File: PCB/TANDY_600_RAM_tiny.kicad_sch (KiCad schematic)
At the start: 5 parts, among them J1 DIN 41612 2x22 male right-ang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, U1 628128_TSOP, U2 74HC08

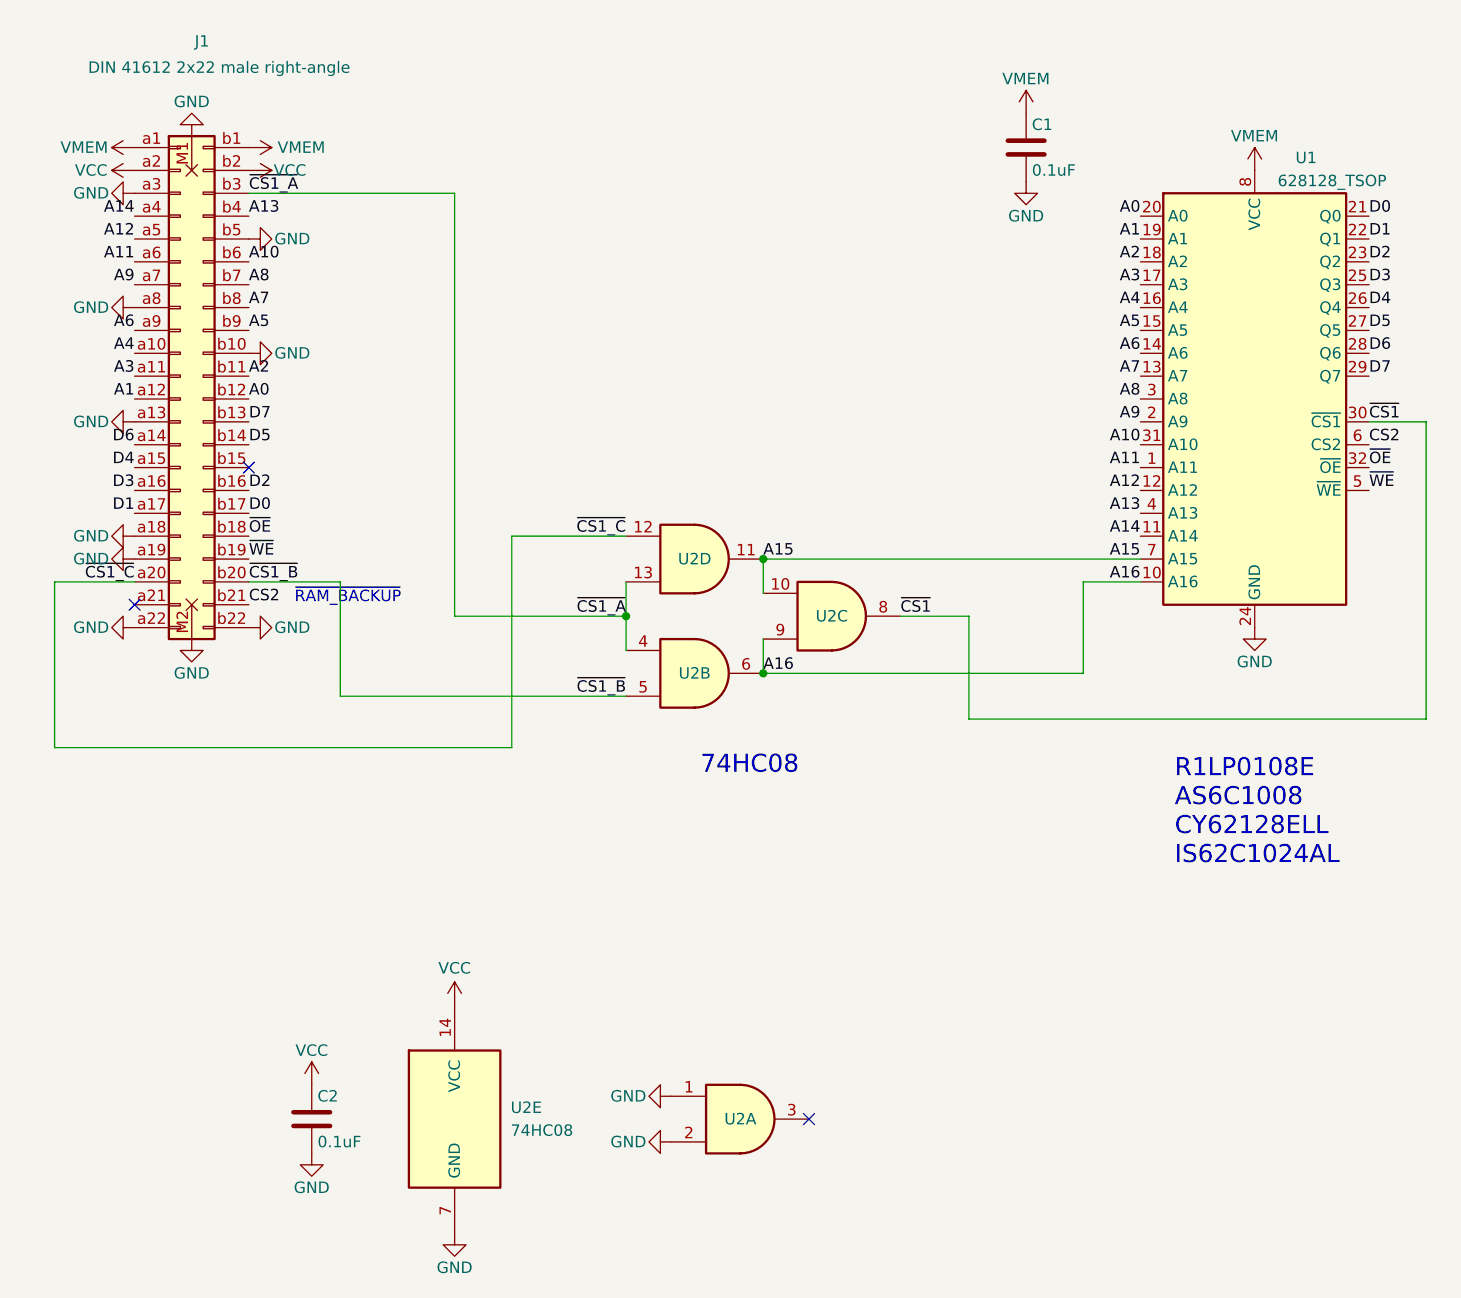
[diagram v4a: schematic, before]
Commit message: footprints on tiny
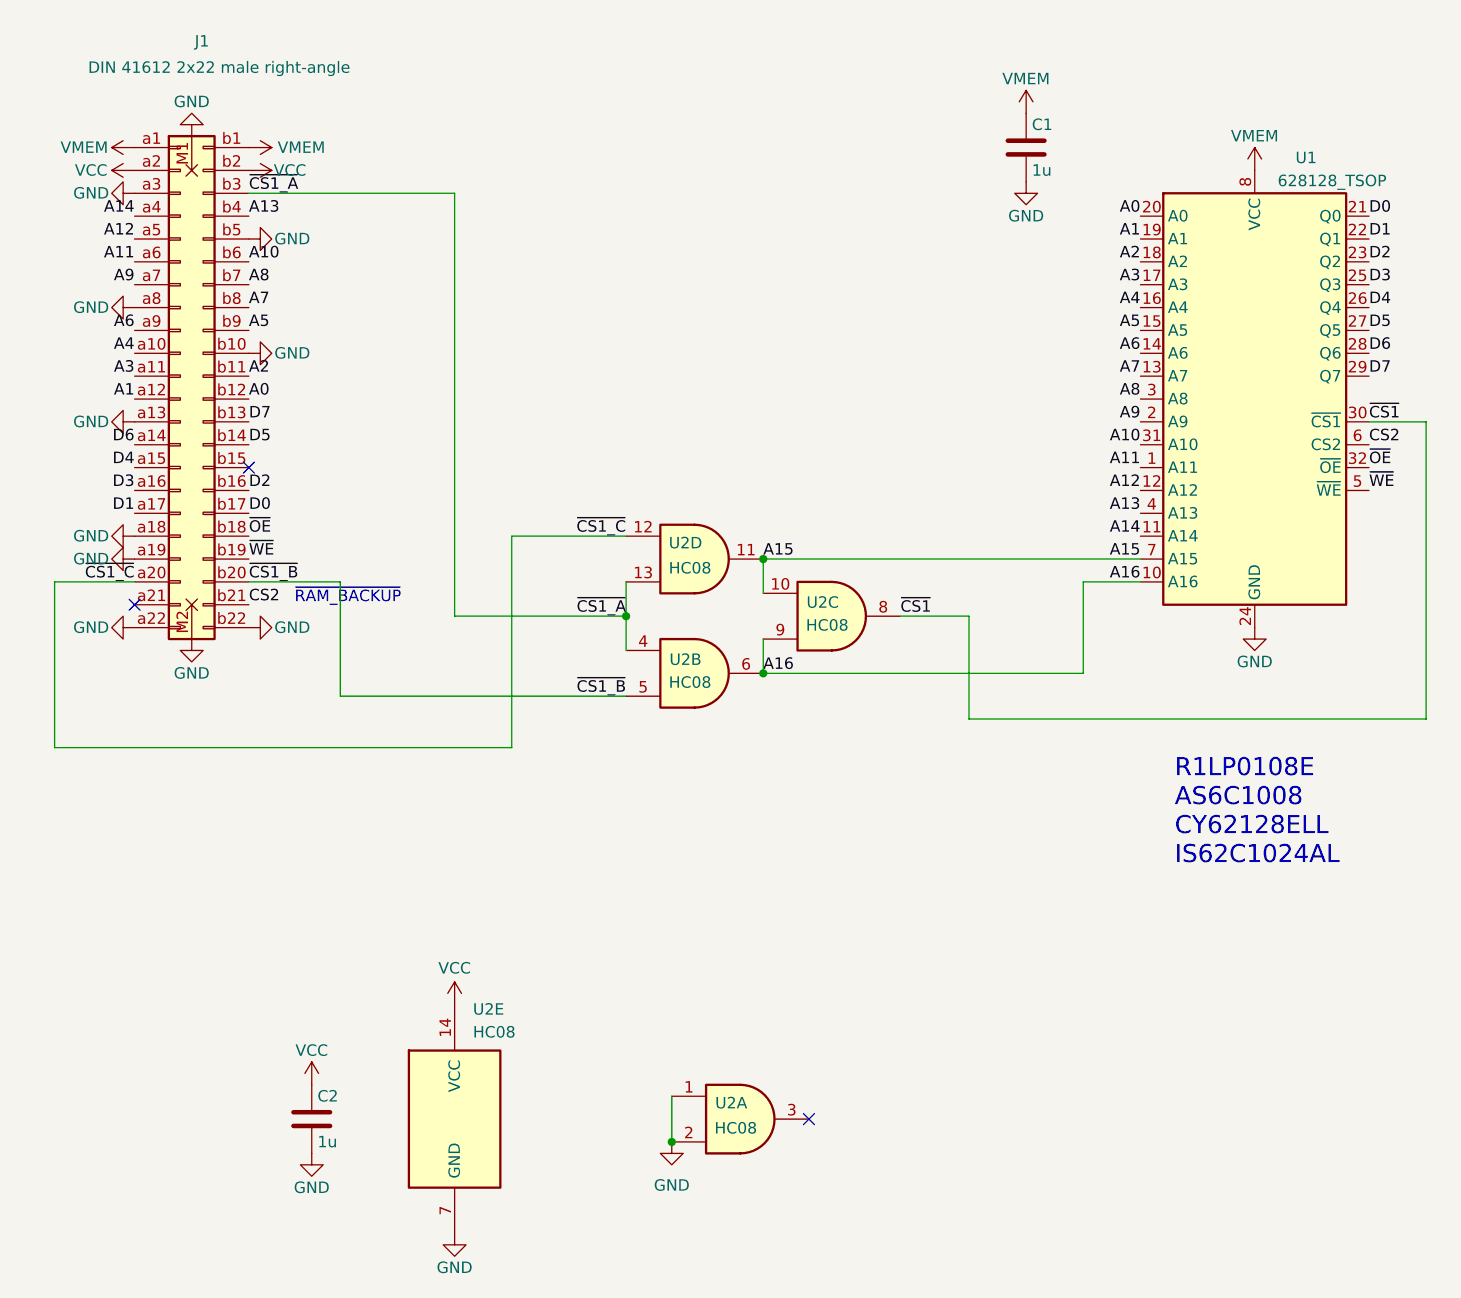
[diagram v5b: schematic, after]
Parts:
- C1, C2: value 0.1uF -> 1u
- U2: value 74HC08 -> HC08
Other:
- note removed: "74HC08"

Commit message: datasheets OPRM pinout
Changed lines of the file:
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@@
 (kicad_sch
-	(version 20231120)
+	(version 20250114)
 	(generator "eeschema")
-	(generator_version "8.0")
+	(generator_version "9.0")
 	(paper "USLetter")
 	(title_block
@@
 		(comment 3 "Replaces TANDY Cat. No. 26-3910 \"OPRM\"")
 	)
+	(text "~{RAM_BACKUP}"
+		(exclude_from_sim no)
+		(at 83.82 101.6 0)
+		(effects
+			(font
+				(size 1.27 1.27)
+			)
+			(justify left bottom)
+		)
+	)
+	(text "R1LP0108E\nAS6C1008\nCY62128ELL\nIS62C1024AL\n"
+		(exclude_from_sim no)
+		(at 181.61 130.683 0)
+		(effects
+			(font
+				(size 2 2)
+			)
+			(justify left bottom)
+		)
+	)
 	(junction
 		(at 135.89 96.52)
@@
 		)
 	)
-	(text "~{RAM_BACKUP}"
-		(exclude_from_sim no)
-		(at 83.82 101.6 0)
-		(effects
-			(font
-				(size 1.27 1.27)
-			)
-			(justify left bottom)
-		)
-	)
-	(text "R1LP0108E\nAS6C1008\nCY62128ELL\nIS62C1024AL\n"
-		(exclude_from_sim no)
-		(at 181.61 130.683 0)
-		(effects
-			(font
-				(size 2 2)
-			)
-			(justify left bottom)
-		)
-	)
 	(label "D2"
 		(at 78.74 88.9 0)
-		(fields_autoplaced yes)
 		(effects
 			(font
@@
 	(label "~{CS1_C}"
 		(at 66.04 99.06 180)
-		(fields_autoplaced yes)
 		(effects
 			(font
@@
 	(label "A13"
 		(at 78.74 58.42 0)
-		(fields_autoplaced yes)
 		(effects
 			(font
@@
 	(label "A15"
 		(at 135.89 96.52 0)
-		(fields_autoplaced yes)
 		(effects
 			(font
@@
 	(label "A12"
 		(at 66.04 60.96 180)
-		(fields_autoplaced yes)
 		(effects
 			(font
@@
 	(label "D6"
 		(at 66.04 83.82 180)
-		(fields_autoplaced yes)
 		(effects
 			(font
@@
 	(label "A13"
 		(at 177.8 91.44 180)
-		(fields_autoplaced yes)
 		(effects
 			(font
@@
 	(label "A7"
 		(at 177.8 76.2 180)
-		(fields_autoplaced yes)
 		(effects
 			(font
@@
 	(label "A16"
 		(at 135.89 109.22 0)
-		(fields_autoplaced yes)
 		(effects
 			(font
@@
 	(label "A1"
 		(at 177.8 60.96 180)
-		(fields_autoplaced yes)
 		(effects
 			(font
@@
 	(label "~{WE}"
 		(at 203.2 88.9 0)
-		(fields_autoplaced yes)
 		(effects
 			(font
@@
 	(label "A4"
 		(at 66.04 73.66 180)
-		(fields_autoplaced yes)
 		(effects
 			(font
@@
 	(label "A3"
 		(at 66.04 76.2 180)
-		(fields_autoplaced yes)
 		(effects
 			(font
@@
 	(label "A4"
 		(at 177.8 68.58 180)
-		(fields_autoplaced yes)
 		(effects
 			(font
@@
 	(label "~{CS1_A}"
 		(at 120.65 102.87 180)
-		(fields_autoplaced yes)
 		(effects
 			(font
@@
 	(label "A12"
 		(at 177.8 88.9 180)
-		(fields_autoplaced yes)
 		(effects
 			(font
@@
 	(label "A9"
 		(at 177.8 81.28 180)
-		(fields_autoplaced yes)
 		(effects
 			(font
@@
 	(label "D0"
 		(at 203.2 58.42 0)
-		(fields_autoplaced yes)
 		(effects
 			(font
@@
 	(label "D0"
 		(at 78.74 91.44 0)
-		(fields_autoplaced yes)
 		(effects
 			(font
@@
 	(label "D7"
 		(at 78.74 81.28 0)
-		(fields_autoplaced yes)
 		(effects
 			(font
@@
 	(label "CS2"
 		(at 78.74 101.6 0)
-		(fields_autoplaced yes)
 		(effects
 			(font
@@
 	(label "A2"
 		(at 78.74 76.2 0)
-		(fields_autoplaced yes)
 		(effects
 			(font
@@
 	(label "D5"
 		(at 203.2 71.12 0)
-		(fields_autoplaced yes)
 		(effects
 			(font
@@
 	(label "A5"
 		(at 177.8 71.12 180)
-		(fields_autoplaced yes)
 		(effects
 			(font
@@
 	(label "A1"
 		(at 66.04 78.74 180)
-		(fields_autoplaced yes)
 		(effects
 			(font
@@
 	(label "~{CS1_A}"
 		(at 78.74 55.88 0)
-		(fields_autoplaced yes)
 		(effects
 			(font
@@
 	(label "CS2"
 		(at 203.2 83.82 0)
-		(fields_autoplaced yes)
 		(effects
 			(font
@@
 	(label "D4"
 		(at 66.04 86.36 180)
-		(fields_autoplaced yes)
 		(effects
 			(font
@@
 	(label "A11"
 		(at 177.8 86.36 180)
-		(fields_autoplaced yes)
 		(effects
 			(font
@@
 	(label "A16"
 		(at 177.8 99.06 180)
-		(fields_autoplaced yes)
 		(effects
 			(font
@@
 	(label "D1"
 		(at 66.04 91.44 180)
-		(fields_autoplaced yes)
 		(effects
 			(font
@@
 	(label "A10"
 		(at 177.8 83.82 180)
-		(fields_autoplaced yes)
 		(effects
 			(font
@@
 	(label "A3"
 		(at 177.8 66.04 180)
-		(fields_autoplaced yes)
 		(effects
 			(font
@@
 	(label "~{CS1_B}"
 		(at 78.74 99.06 0)
-		(fields_autoplaced yes)
 		(effects
 			(font
@@
 	(label "~{CS1_C}"
 		(at 120.65 93.98 180)
-		(fields_autoplaced yes)
 		(effects
 			(font
@@
 	(label "D5"
 		(at 78.74 83.82 0)
-		(fields_autoplaced yes)
 		(effects
 			(font
@@
 	(label "A6"
 		(at 66.04 71.12 180)
-		(fields_autoplaced yes)
 		(effects
 			(font
@@
 	(label "A5"
 		(at 78.74 71.12 0)
-		(fields_autoplaced yes)
 		(effects
 			(font
@@
 	(label "~{OE}"
 		(at 78.74 93.98 0)
-		(fields_autoplaced yes)
 		(effects
 			(font
@@
 	(label "A0"
 		(at 78.74 78.74 0)
-		(fields_autoplaced yes)
 		(effects
 			(font
@@
 	(label "A8"
 		(at 78.74 66.04 0)
-		(fields_autoplaced yes)
 		(effects
 			(font
@@
 	(label "~{CS1}"
 		(at 151.13 102.87 0)
-		(fields_autoplaced yes)
 		(effects
 			(font
@@
 	(label "D1"
 		(at 203.2 60.96 0)
-		(fields_autoplaced yes)
 		(effects
 			(font
@@
 	(label "D3"
 		(at 66.04 88.9 180)
-		(fields_autoplaced yes)
 		(effects
 			(font
@@
 	(label "A14"
 		(at 177.8 93.98 180)
-		(fields_autoplaced yes)
 		(effects
 			(font
@@
 	(label "A10"
 		(at 78.74 63.5 0)
-		(fields_autoplaced yes)
 		(effects
 			(font
@@
 	(label "A11"
 		(at 66.04 63.5 180)
-		(fields_autoplaced yes)
 		(effects
 			(font
@@
 	(label "A2"
 		(at 177.8 63.5 180)
-		(fields_autoplaced yes)
 		(effects
 			(font
@@
 	(label "D7"
 		(at 203.2 76.2 0)
-		(fields_autoplaced yes)
 		(effects
 			(font
@@
 	(label "A14"
 		(at 66.04 58.42 180)
-		(fields_autoplaced yes)
 		(effects
 			(font
@@
 	(label "A8"
 		(at 177.8 78.74 180)
-		(fields_autoplaced yes)
 		(effects
 			(font
@@
 	(label "D2"
 		(at 203.2 63.5 0)
-		(fields_autoplaced yes)
 		(effects
 			(font
@@
 	(label "D3"
 		(at 203.2 66.04 0)
-		(fields_autoplaced yes)
 		(effects
 			(font
@@
 	(label "A7"
 		(at 78.74 68.58 0)
-		(fields_autoplaced yes)
 		(effects
 			(font
@@
 	(label "A15"
 		(at 177.8 96.52 180)
-		(fields_autoplaced yes)
 		(effects
 			(font
@@
 	(label "~{CS1_B}"
 		(at 120.65 111.76 180)
-		(fields_autoplaced yes)
 		(effects
 			(font
@@
 	(label "A0"
 		(at 177.8 58.42 180)
-		(fields_autoplaced yes)
 		(effects
 			(font
@@
 	(label "A9"
 		(at 66.04 66.04 180)
-		(fields_autoplaced yes)
 		(effects
 			(font
@@
 	(label "~{OE}"
 		(at 203.2 86.36 0)
-		(fields_autoplaced yes)
 		(effects
 			(font
@@
 	(label "A6"
 		(at 177.8 73.66 180)
-		(fields_autoplaced yes)
 		(effects
 			(font
@@
 	(label "~{CS1}"
 		(at 203.2 81.28 0)
-		(fields_autoplaced yes)
 		(effects
 			(font
@@
 	(label "D4"
 		(at 203.2 68.58 0)
-		(fields_autoplaced yes)
 		(effects
 			(font
@@
 	(label "D6"
 		(at 203.2 73.66 0)
-		(fields_autoplaced yes)
 		(effects
 			(font
@@
 	(label "~{WE}"
 		(at 78.74 96.52 0)
-		(fields_autoplaced yes)
 		(effects
 			(font
@@
 			)
 		)
-		(property "Datasheet" "~"
+		(property "Datasheet" "datasheets/TANDY_600_OPRM.pdf"
 			(at 71.12 76.2 0)
 			(effects
@@
 		)
 	)
+	(embedded_fonts no)
 )
